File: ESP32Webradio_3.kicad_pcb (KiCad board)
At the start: 2 copper layers, 51.6 x 54.5 mm, 17 parts, among them J1 5V, J2 Rot, J3 Display, J5 SJ1-3523N, U1 esp32_38_pins-custom_library

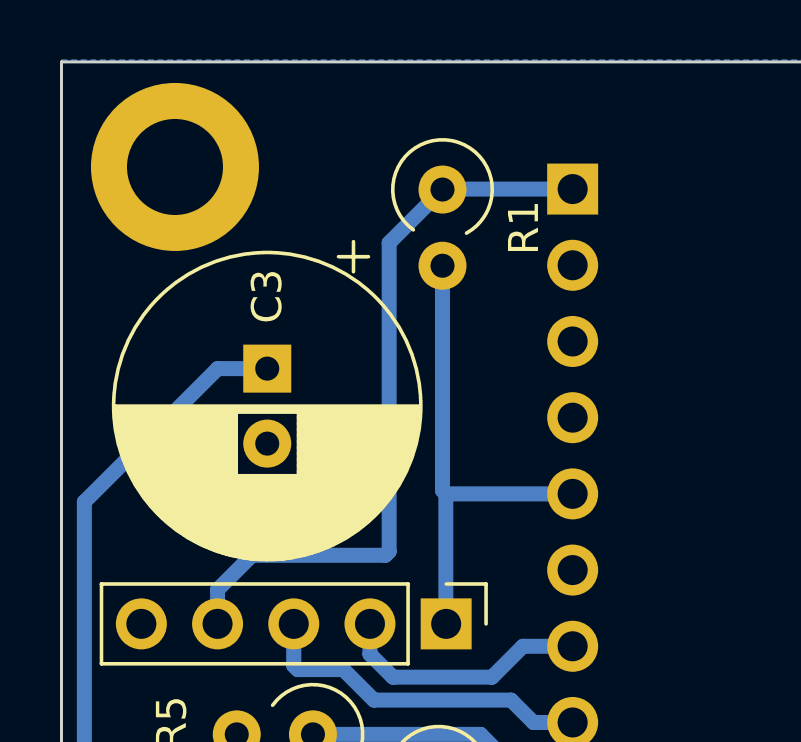
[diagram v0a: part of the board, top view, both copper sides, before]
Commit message: flash witout button capacitor added
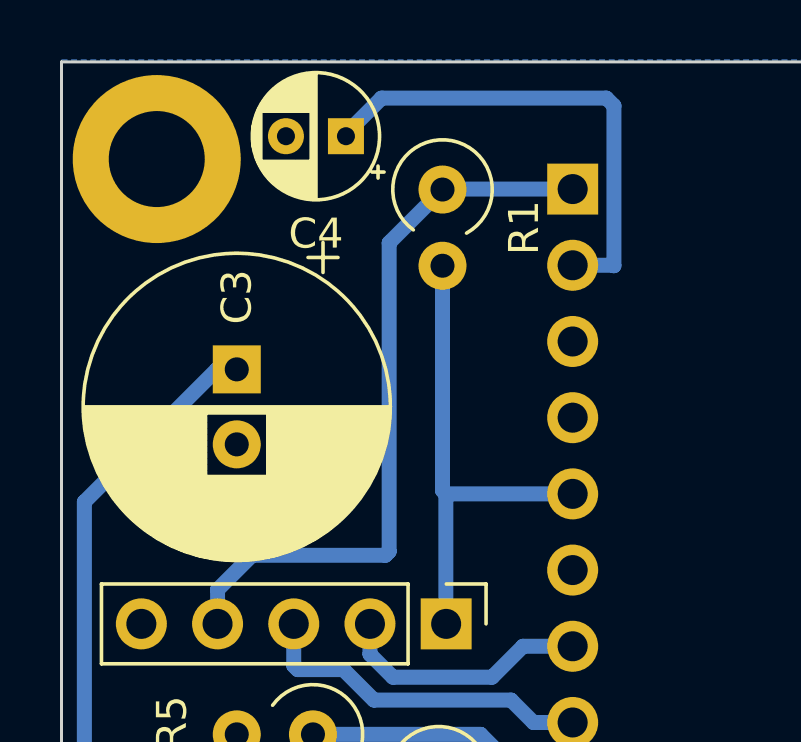
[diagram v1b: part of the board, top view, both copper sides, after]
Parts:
- added C4: 10yF, Capacitor_THT:CP_Radial_D4.0mm_P2.00mm, F.Cu at (94.7, 66.9)
- moved C3 1.02 mm to (91.1, 74.7)
- moved H1 0.66 mm to (88.4, 67.7)
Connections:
- U1 pad 2: unconnected-(U1-Pad2) -> Net-(U1-Pad2)
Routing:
- net Net-(U1-Pad2): track 0.00 -> 16.3 mm
- net +5V: track 132.0 -> 131.0 mm

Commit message: clear circuits
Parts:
- moved R5 5.21 mm to (88.4, 87.1), turned to -90 degrees
- moved C2 1.59 mm to (91.6, 89.7)
- moved R2 1.53 mm to (98.4, 89.7)
- moved R4 1.50 mm to (88.4, 93.7)
- moved C1 1.40 mm to (96.1, 95.8)
- moved R3 1.40 mm to (96.0, 100.3)
- moved C4 1.05 mm to (94.0, 66.2), turned to -90 degrees
- moved H4 0.31 mm to (133.5, 67.7)
- moved R1 0.25 mm to (98.2, 68.7)
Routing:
- net Net-(R5-Pad1): track 9.54 -> 14.4 mm
- net Net-(R2-Pad1): track 5.83 -> 4.20 mm
- net Net-(C2-Pad1): track 8.83 -> 7.26 mm
- net /S: track 15.2 -> 13.8 mm
- net /R: track 21.7 -> 22.7 mm
- net Net-(C4-Pad1): track 16.3 -> 15.3 mm
